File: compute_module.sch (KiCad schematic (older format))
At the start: 14 parts, among them Q1 2N7002P.215

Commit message: Assigned footprints to most components
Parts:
- C1, C2, C3, C4, C5, C6, C7, C8: footprint (none) -> Capacitors_SMD:C_0603_HandSoldering
- D1: footprint (none) -> LEDs:LED_0805
- Q1: footprint (none) -> TO_SOT_Packages_SMD:SOT-23
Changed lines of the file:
@@
 F 0 "C3" H 4550 7000 50  0000 L CNN
 F 1 "100nF" V 4450 7150 50  0000 L CNN
-F 2 "" H 4538 6950 50  0000 C CNN
+F 2 "Capacitors_SMD:C_0603_HandSoldering" H 4538 6950 50  0001 C CNN
 F 3 "" H 4500 7100 50  0000 C CNN
 	1    4500 7100
@@
 F 0 "C4" H 4750 7000 50  0000 L CNN
 F 1 "100nF" V 4650 7150 50  0000 L CNN
-F 2 "" H 4738 6950 50  0000 C CNN
+F 2 "Capacitors_SMD:C_0603_HandSoldering" H 4738 6950 50  0001 C CNN
 F 3 "" H 4700 7100 50  0000 C CNN
 	1    4700 7100
@@
 F 0 "C1" H 4050 7000 50  0000 L CNN
 F 1 "100nF" V 3950 7150 50  0000 L CNN
-F 2 "" H 4038 6950 50  0000 C CNN
+F 2 "Capacitors_SMD:C_0603_HandSoldering" H 4038 6950 50  0001 C CNN
 F 3 "" H 4000 7100 50  0000 C CNN
 	1    4000 7100
@@
 F 0 "C2" H 4250 7000 50  0000 L CNN
 F 1 "100nF" V 4150 7150 50  0000 L CNN
-F 2 "" H 4238 6950 50  0000 C CNN
+F 2 "Capacitors_SMD:C_0603_HandSoldering" H 4238 6950 50  0001 C CNN
 F 3 "" H 4200 7100 50  0000 C CNN
 	1    4200 7100
@@
 F 0 "C5" H 5050 7000 50  0000 L CNN
 F 1 "100nF" V 4950 7150 50  0000 L CNN
-F 2 "" H 5038 6950 50  0000 C CNN
+F 2 "Capacitors_SMD:C_0603_HandSoldering" H 5038 6950 50  0001 C CNN
 F 3 "" H 5000 7100 50  0000 C CNN
 	1    5000 7100
@@
 F 0 "C6" H 5250 7000 50  0000 L CNN
 F 1 "100nF" V 5150 7150 50  0000 L CNN
-F 2 "" H 5238 6950 50  0000 C CNN
+F 2 "Capacitors_SMD:C_0603_HandSoldering" H 5238 6950 50  0001 C CNN
 F 3 "" H 5200 7100 50  0000 C CNN
 	1    5200 7100
@@
 F 0 "C7" H 5550 7000 50  0000 L CNN
 F 1 "100nF" V 5450 7150 50  0000 L CNN
-F 2 "" H 5538 6950 50  0000 C CNN
+F 2 "Capacitors_SMD:C_0603_HandSoldering" H 5538 6950 50  0001 C CNN
 F 3 "" H 5500 7100 50  0000 C CNN
 	1    5500 7100
@@
 F 0 "C8" H 5750 7000 50  0000 L CNN
 F 1 "100nF" V 5650 7150 50  0000 L CNN
-F 2 "" H 5738 6950 50  0000 C CNN
+F 2 "Capacitors_SMD:C_0603_HandSoldering" H 5738 6950 50  0001 C CNN
 F 3 "" H 5700 7100 50  0000 C CNN
 	1    5700 7100
@@
 F 0 "D1" H 4100 1600 50  0000 C CNN
 F 1 "LED" H 4100 1400 50  0000 C CNN
-F 2 "" H 4100 1500 50  0000 C CNN
+F 2 "LEDs:LED_0805" H 4100 1500 50  0001 C CNN
 F 3 "" H 4100 1500 50  0000 C CNN
 	1    4100 1500
@@
 F 0 "Q1" H 3900 2200 50  0000 L CNN
 F 1 "2N7002P.215" V 4250 1800 50  0000 L CNN
-F 2 "" H 4200 2150 50  0000 C CNN
+F 2 "TO_SOT_Packages_SMD:SOT-23" H 4200 2150 50  0001 C CNN
 F 3 "" H 4000 2050 50  0000 C CNN
 	1    4000 2050

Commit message: Laid down components
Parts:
- C1, C2, C3, C4, C5, C6, C7, C8: footprint Capacitors_SMD:C_0603_HandSoldering -> Capacitors_SMD:C_0402
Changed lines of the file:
@@
 F 0 "C3" H 4550 7000 50  0000 L CNN
 F 1 "100nF" V 4450 7150 50  0000 L CNN
-F 2 "Capacitors_SMD:C_0603_HandSoldering" H 4538 6950 50  0001 C CNN
+F 2 "Capacitors_SMD:C_0402" H 4538 6950 50  0001 C CNN
 F 3 "" H 4500 7100 50  0000 C CNN
 	1    4500 7100
@@
 F 0 "C4" H 4750 7000 50  0000 L CNN
 F 1 "100nF" V 4650 7150 50  0000 L CNN
-F 2 "Capacitors_SMD:C_0603_HandSoldering" H 4738 6950 50  0001 C CNN
+F 2 "Capacitors_SMD:C_0402" H 4738 6950 50  0001 C CNN
 F 3 "" H 4700 7100 50  0000 C CNN
 	1    4700 7100
@@
 F 0 "C1" H 4050 7000 50  0000 L CNN
 F 1 "100nF" V 3950 7150 50  0000 L CNN
-F 2 "Capacitors_SMD:C_0603_HandSoldering" H 4038 6950 50  0001 C CNN
+F 2 "Capacitors_SMD:C_0402" H 4038 6950 50  0001 C CNN
 F 3 "" H 4000 7100 50  0000 C CNN
 	1    4000 7100
@@
 F 0 "C2" H 4250 7000 50  0000 L CNN
 F 1 "100nF" V 4150 7150 50  0000 L CNN
-F 2 "Capacitors_SMD:C_0603_HandSoldering" H 4238 6950 50  0001 C CNN
+F 2 "Capacitors_SMD:C_0402" H 4238 6950 50  0001 C CNN
 F 3 "" H 4200 7100 50  0000 C CNN
 	1    4200 7100
@@
 F 0 "C5" H 5050 7000 50  0000 L CNN
 F 1 "100nF" V 4950 7150 50  0000 L CNN
-F 2 "Capacitors_SMD:C_0603_HandSoldering" H 5038 6950 50  0001 C CNN
+F 2 "Capacitors_SMD:C_0402" H 5038 6950 50  0001 C CNN
 F 3 "" H 5000 7100 50  0000 C CNN
 	1    5000 7100
@@
 F 0 "C6" H 5250 7000 50  0000 L CNN
 F 1 "100nF" V 5150 7150 50  0000 L CNN
-F 2 "Capacitors_SMD:C_0603_HandSoldering" H 5238 6950 50  0001 C CNN
+F 2 "Capacitors_SMD:C_0402" H 5238 6950 50  0001 C CNN
 F 3 "" H 5200 7100 50  0000 C CNN
 	1    5200 7100
@@
 F 0 "C7" H 5550 7000 50  0000 L CNN
 F 1 "100nF" V 5450 7150 50  0000 L CNN
-F 2 "Capacitors_SMD:C_0603_HandSoldering" H 5538 6950 50  0001 C CNN
+F 2 "Capacitors_SMD:C_0402" H 5538 6950 50  0001 C CNN
 F 3 "" H 5500 7100 50  0000 C CNN
 	1    5500 7100
@@
 F 0 "C8" H 5750 7000 50  0000 L CNN
 F 1 "100nF" V 5650 7150 50  0000 L CNN
-F 2 "Capacitors_SMD:C_0603_HandSoldering" H 5738 6950 50  0001 C CNN
+F 2 "Capacitors_SMD:C_0402" H 5738 6950 50  0001 C CNN
 F 3 "" H 5700 7100 50  0000 C CNN
 	1    5700 7100

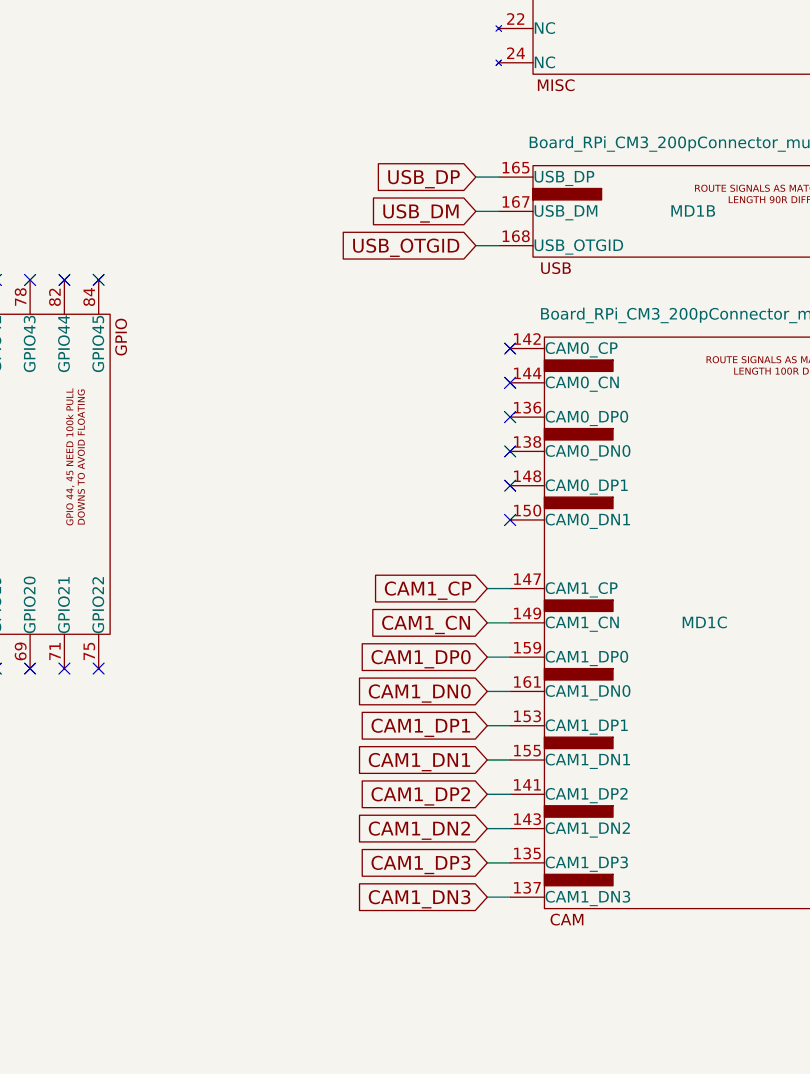
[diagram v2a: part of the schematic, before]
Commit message: Routed differential pairs for camera and HDMI
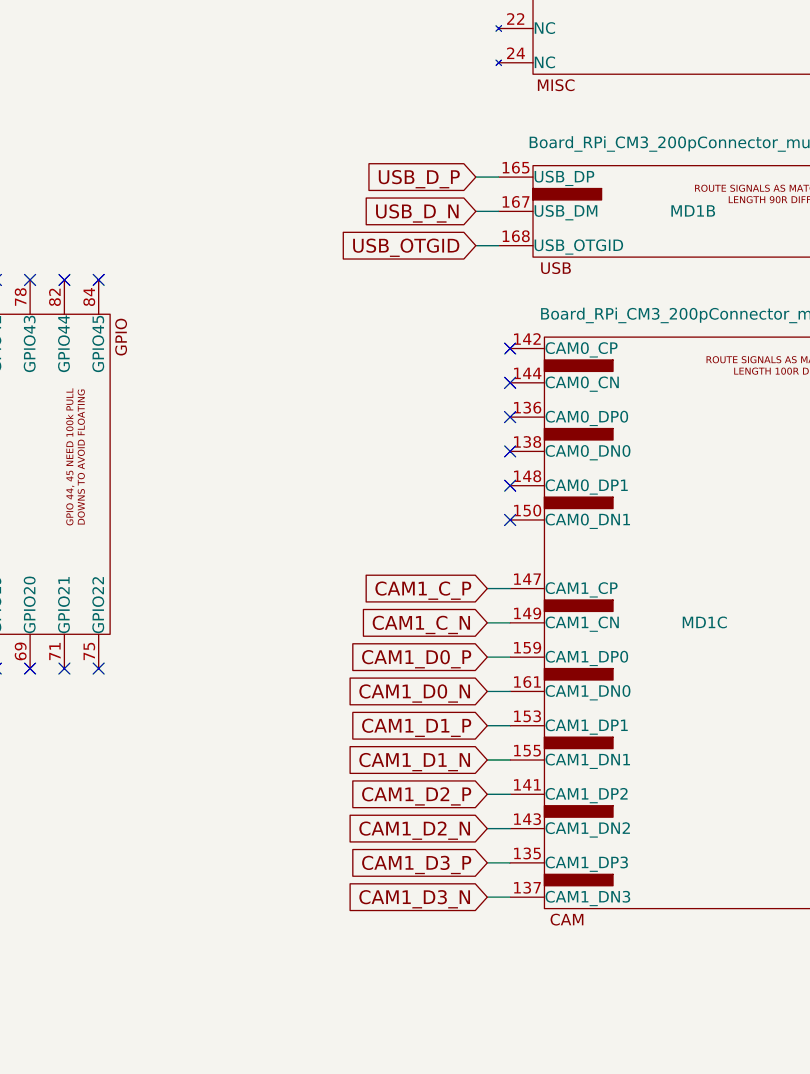
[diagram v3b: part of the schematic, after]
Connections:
- net CAM1_CN renamed CAM1_C_N
- net CAM1_CP renamed CAM1_C_P
- net CAM1_DN0 renamed CAM1_D0_N
- net CAM1_DN1 renamed CAM1_D1_N
- net CAM1_DN2 renamed CAM1_D2_N
- net CAM1_DN3 renamed CAM1_D3_N
- net CAM1_DP0 renamed CAM1_D0_P
- net CAM1_DP1 renamed CAM1_D1_P
- net CAM1_DP2 renamed CAM1_D2_P
- net CAM1_DP3 renamed CAM1_D3_P
- net USB_DM renamed USB_D_N
- net USB_DP renamed USB_D_P
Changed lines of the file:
@@
 $EndComp
 Text GLabel 9350 3200 0    60   Input ~ 0
-USB_DP
+USB_D_P
 Text GLabel 9350 3350 0    60   Input ~ 0
-USB_DM
+USB_D_N
 Text GLabel 6450 1050 2    60   Input ~ 0
 HDMI_CLK_N
@@
 CAM1_IO0
 Text GLabel 9400 5000 0    60   Input ~ 0
-CAM1_CP
+CAM1_C_P
 Text GLabel 9400 5150 0    60   Input ~ 0
-CAM1_CN
+CAM1_C_N
 Text GLabel 9400 5300 0    60   Input ~ 0
-CAM1_DP0
+CAM1_D0_P
 Text GLabel 9400 5450 0    60   Input ~ 0
-CAM1_DN0
+CAM1_D0_N
 Text GLabel 9400 5600 0    60   Input ~ 0
-CAM1_DP1
+CAM1_D1_P
 Text GLabel 9400 5750 0    60   Input ~ 0
-CAM1_DN1
+CAM1_D1_N
 Text GLabel 9400 5900 0    60   Input ~ 0
-CAM1_DP2
+CAM1_D2_P
 Text GLabel 9400 6050 0    60   Input ~ 0
-CAM1_DN2
+CAM1_D2_N
 Text GLabel 9400 6200 0    60   Input ~ 0
-CAM1_DP3
+CAM1_D3_P
 Text GLabel 9400 6350 0    60   Input ~ 0
-CAM1_DN3
+CAM1_D3_N
 $Sheet
 S 6050 6500 600  500

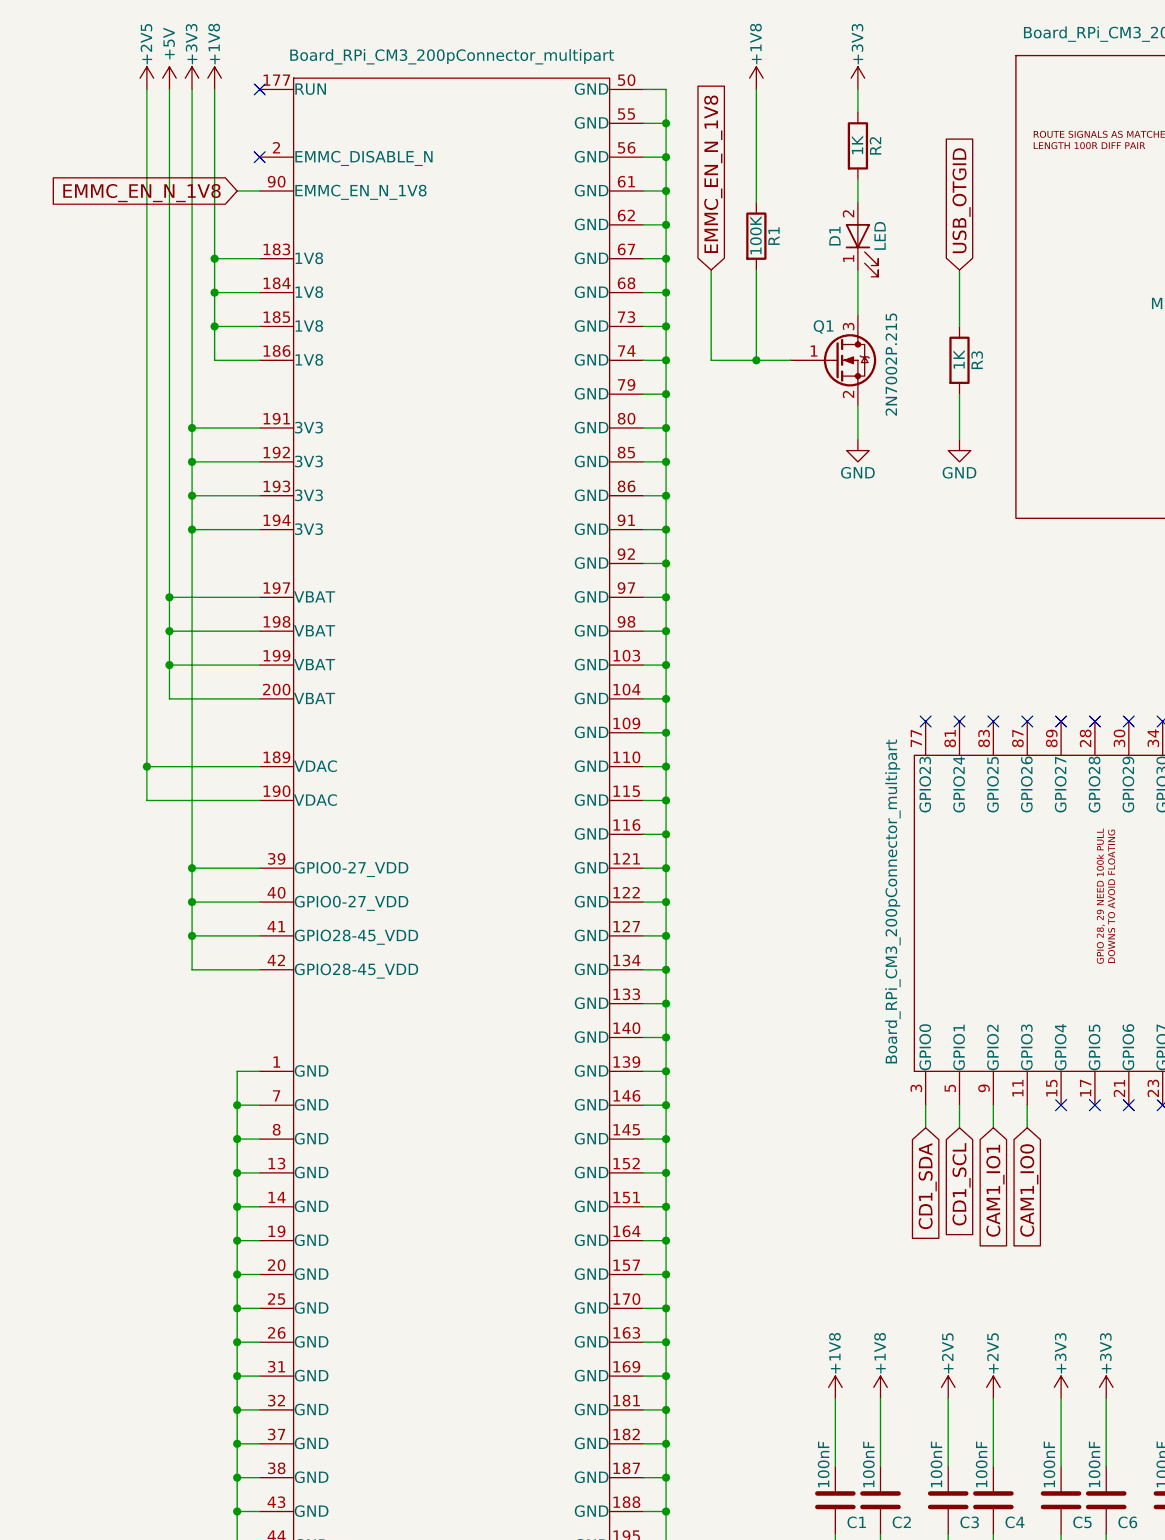
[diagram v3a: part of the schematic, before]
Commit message: Removed 2.5V regulator and changed bottom ground plane clearence
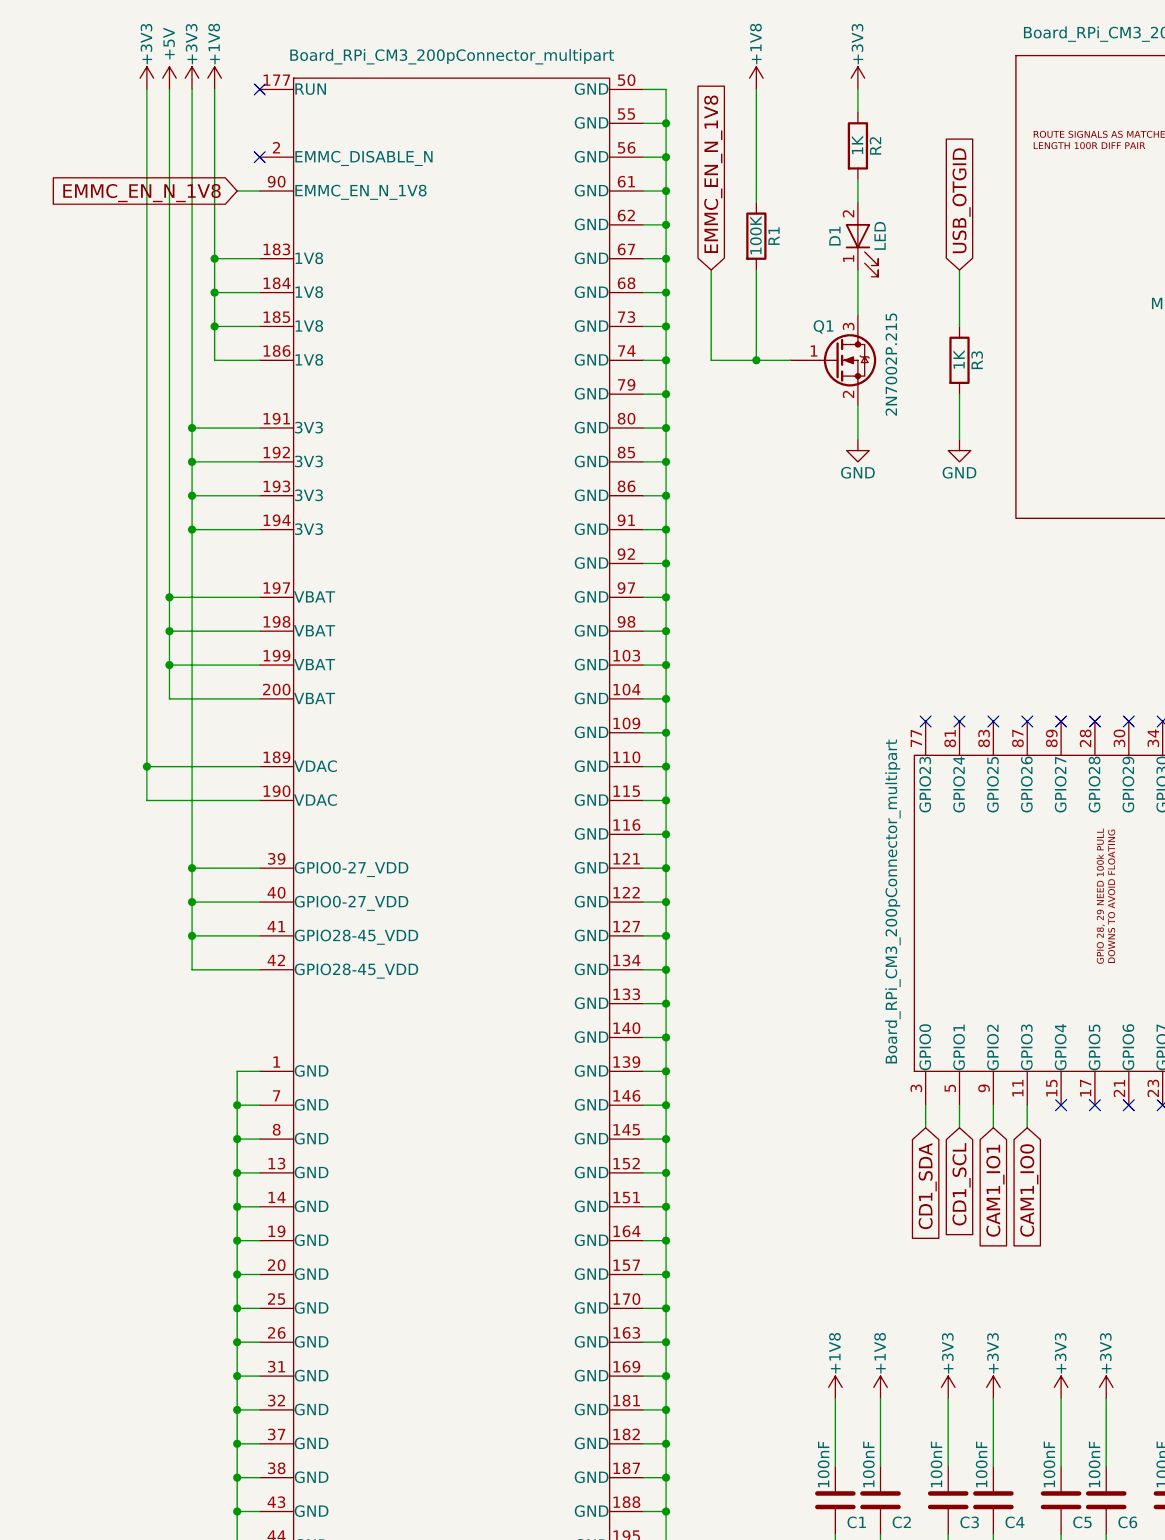
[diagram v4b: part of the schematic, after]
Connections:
- net +2V5 is gone; now on net +3V3: C3.1, C4.1, MD1.189 (VDAC), MD1.190 (VDAC)
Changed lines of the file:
@@
-	1    0    0    -1
-$EndComp
-$Comp
-L +2V5 #PWR06
-U 1 1 5C0F559A
-P 950 850
-F 0 "#PWR06" H 950 700 50  0001 C CNN
-F 1 "+2V5" V 950 1050 50  0000 C CNN
-F 2 "" H 950 850 50  0000 C CNN
-F 3 "" H 950 850 50  0000 C CNN
-	1    950  850
 	1    0    0    -1
 $EndComp
@@
 $EndComp
 $Comp
-L +2V5 #PWR020
-U 1 1 5C11C500
-P 4700 6650
-F 0 "#PWR020" H 4700 6500 50  0001 C CNN
-F 1 "+2V5" V 4700 6850 50  0000 C CNN
-F 2 "" H 4700 6650 50  0000 C CNN
-F 3 "" H 4700 6650 50  0000 C CNN
-	1    4700 6650
-	1    0    0    -1
-$EndComp
-$Comp
 L C C3
 U 1 1 5C11C67C
@@
 F 3 "" H 4500 7600 50  0000 C CNN
 	1    4500 7600
-	1    0    0    -1
-$EndComp
-$Comp
-L +2V5 #PWR022
-U 1 1 5C11C68A
-P 4500 6650
-F 0 "#PWR022" H 4500 6500 50  0001 C CNN
-F 1 "+2V5" V 4500 6850 50  0000 C CNN
-F 2 "" H 4500 6650 50  0000 C CNN
-F 3 "" H 4500 6650 50  0000 C CNN
-	1    4500 6650
 	1    0    0    -1
 $EndComp
@@
 Wire Wire Line
 	3650 850  3650 1350
+$Comp
+L +3V3 #PWR?
+U 1 1 5C195AE7
+P 950 850
+F 0 "#PWR?" H 950 700 50  0001 C CNN
+F 1 "+3V3" V 950 1050 50  0000 C CNN
+F 2 "" H 950 850 50  0000 C CNN
+F 3 "" H 950 850 50  0000 C CNN
+	1    950  850
+	1    0    0    -1
+$EndComp
+$Comp
+L +3V3 #PWR?
+U 1 1 5C195EED
+P 4700 6650
+F 0 "#PWR?" H 4700 6500 50  0001 C CNN
+F 1 "+3V3" V 4700 6850 50  0000 C CNN
+F 2 "" H 4700 6650 50  0000 C CNN
+F 3 "" H 4700 6650 50  0000 C CNN
+	1    4700 6650
+	1    0    0    -1
+$EndComp
+$Comp
+L +3V3 #PWR?
+U 1 1 5C195F34
+P 4500 6650
+F 0 "#PWR?" H 4500 6500 50  0001 C CNN
+F 1 "+3V3" V 4500 6850 50  0000 C CNN
+F 2 "" H 4500 6650 50  0000 C CNN
+F 3 "" H 4500 6650 50  0000 C CNN
+	1    4500 6650
+	1    0    0    -1
+$EndComp
 $EndSCHEMATC

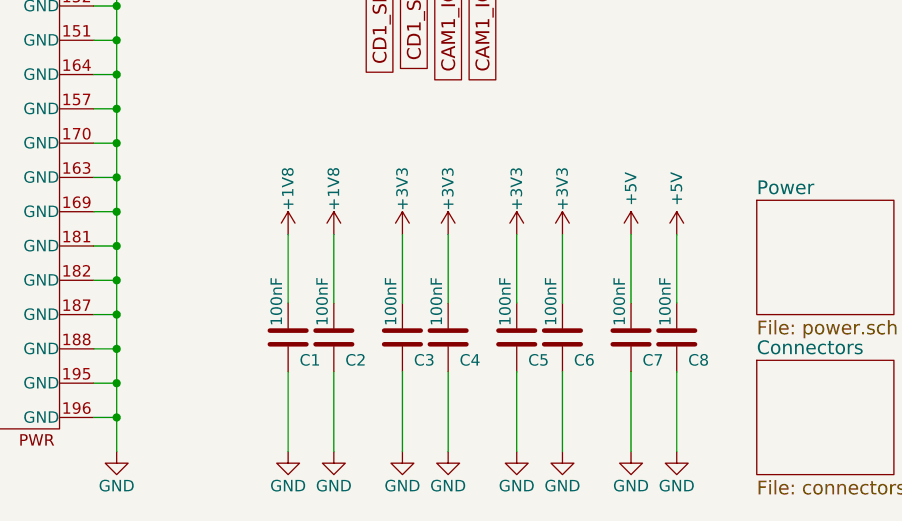
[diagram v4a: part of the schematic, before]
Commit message: Added decoupling caps for gpio power pins
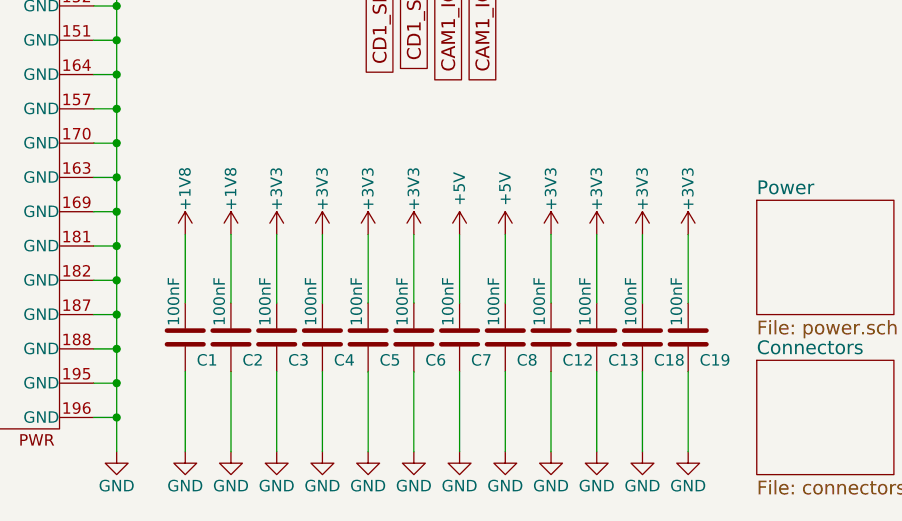
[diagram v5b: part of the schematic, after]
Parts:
- added C12, C13, C18, C19: 100nF, Capacitors_SMD:C_0402, symbol C
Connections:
- net +3V3: now also C12.1, C13.1, C18.1, C19.1
- net GND: now also C12.2, C13.2, C18.2, C19.2
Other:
- moved on the sheet: C1, C2, C3, C4, C5, C6, C7, C8
